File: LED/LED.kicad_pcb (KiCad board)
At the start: 2 copper layers, 68 x 68 mm, 17 parts, among them J1 BM03B-SRSS-TBT_LF__SN_, Q1 AO3400A, U1 PESD3V3U1UL_315

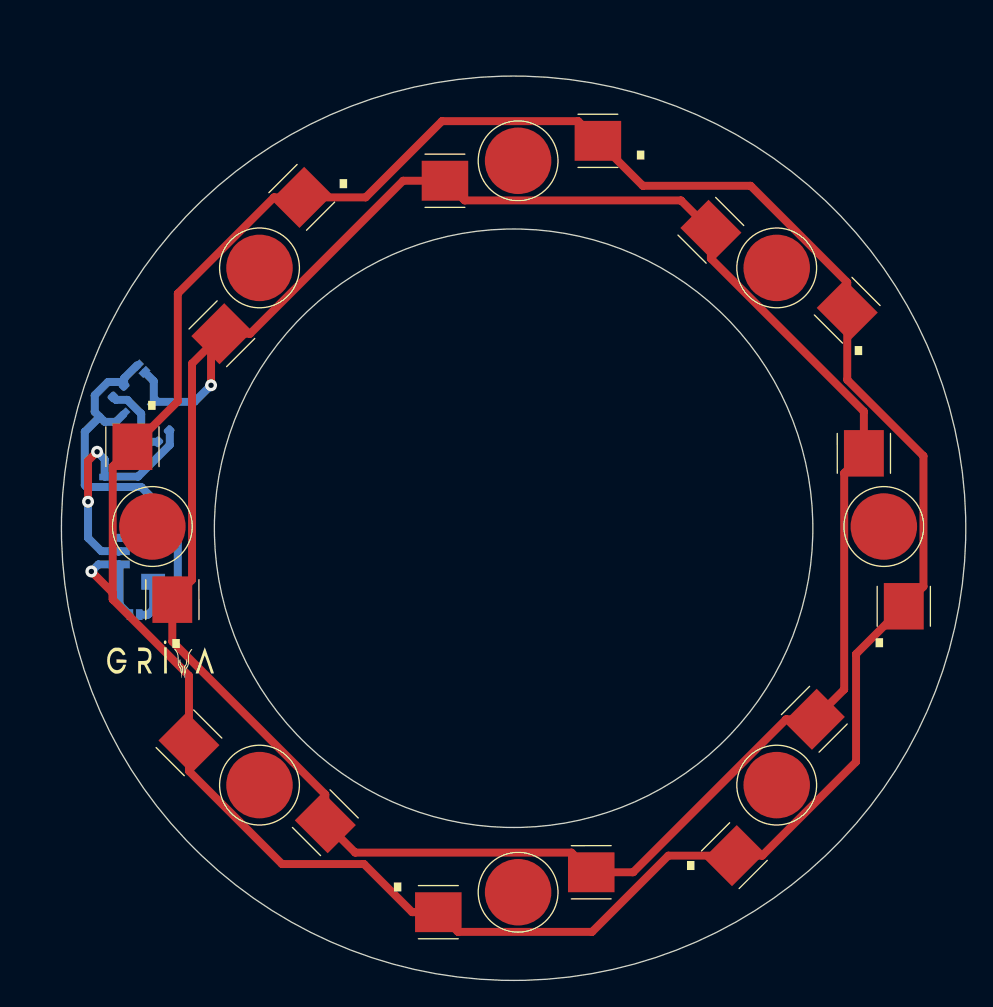
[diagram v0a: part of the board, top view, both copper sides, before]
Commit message: changed footprint for proper placement of components
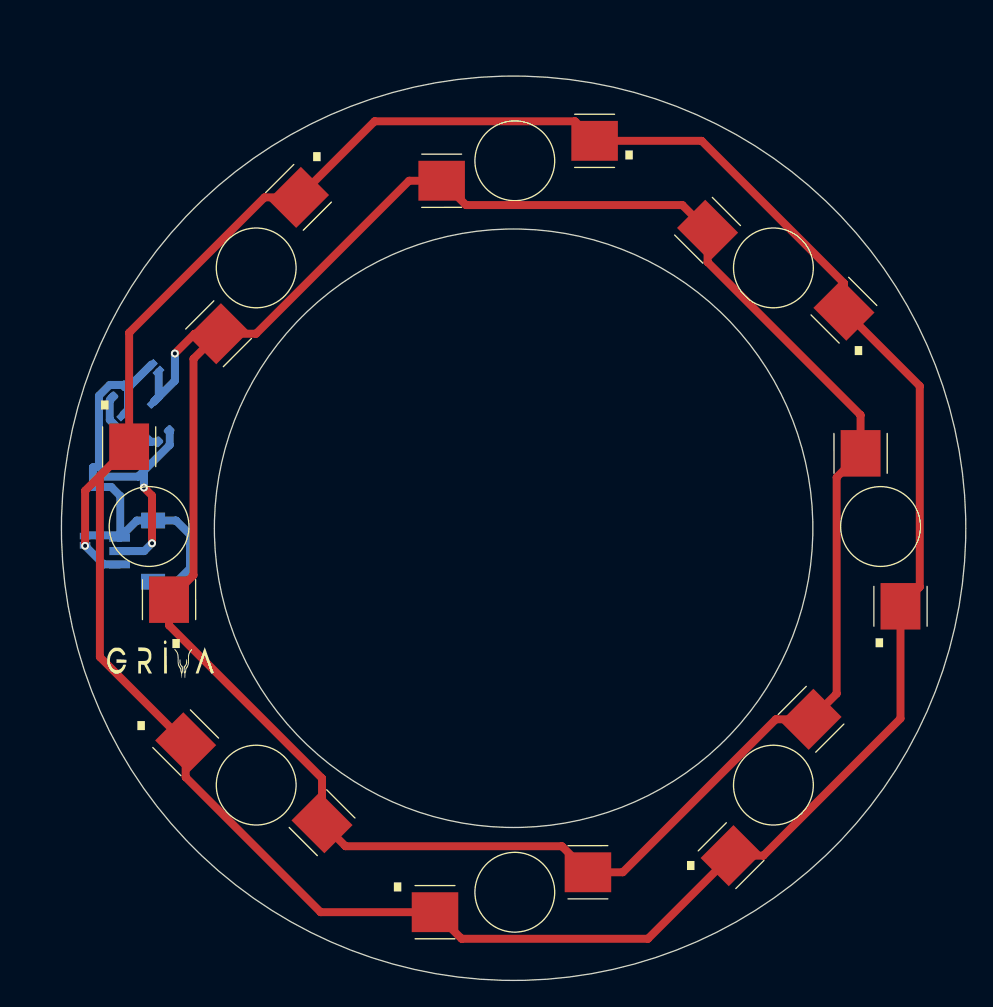
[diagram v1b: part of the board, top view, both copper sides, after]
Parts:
- moved D10 6.69 mm to (111.3, 97.4), turned to 90 degrees
- moved D9 1.05 mm to (116.5, 84.5)
- moved D1 0.25 mm to (143.6, 68.9)
- moved D2 0.25 mm to (163.0, 76.9)
- moved D3 0.25 mm to (171.1, 96.4)
- moved D4 0.25 mm to (163.0, 115.8)
- moved D5 0.25 mm to (143.6, 123.9)
- moved D6 0.25 mm to (124.1, 115.8)
- moved D7 0.25 mm to (116.1, 96.4)
- moved D8 0.25 mm to (124.1, 76.9)
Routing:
- net VCC: track 212.1 -> 215.7 mm
- net Gate: track 18.7 -> 15.4 mm
- net Drain: track 183.9 -> 182.9 mm
- net Net-(Q1-Pad1): track 5.60 -> 6.51 mm
- net GND: track 35.7 -> 34.9 mm
